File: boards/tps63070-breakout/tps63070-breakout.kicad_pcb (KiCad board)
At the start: 2 copper layers, 24.7 x 22.9 mm, 15 parts, among them J1 MODULE PINS, U1 TPS63070

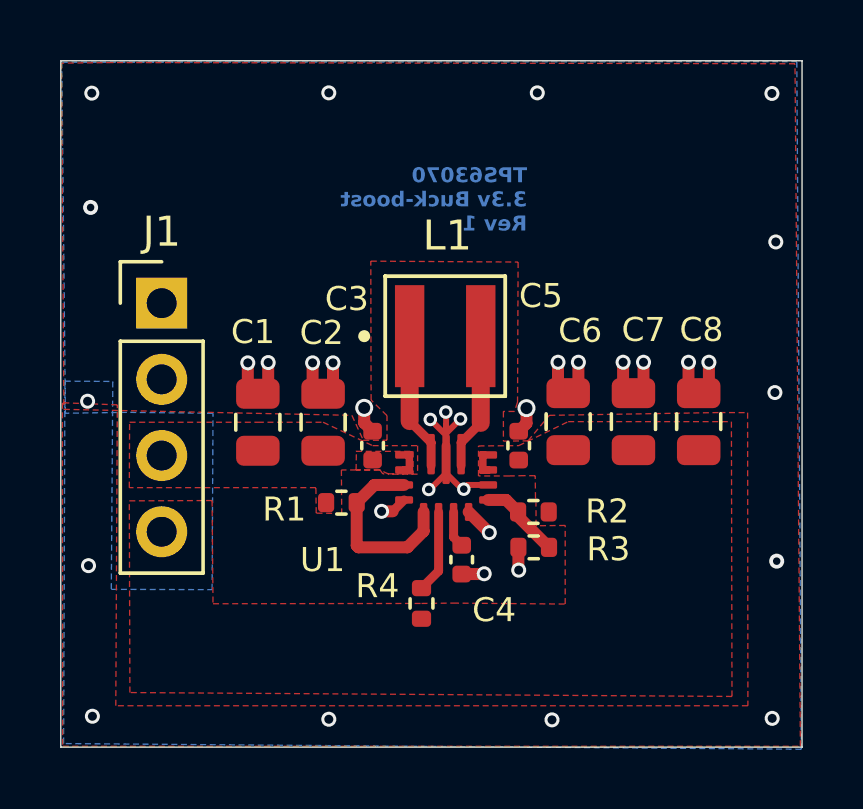
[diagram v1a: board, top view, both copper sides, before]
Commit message: fix: correct TPS63070 symbol pin types and update board docs (#24)
* fix: correct TPS63070 symbol pin types, update board README

Symbol library changes:
- VOUT pins 7/8: power_in → power_out/passive (it outputs power)
- L1/L2 pins 11/9: unspecified → passive (inductor connections)
- VAUX pin 3: unspecified → power_out (auxiliary supply)
- PGND pin 10: power_in → passive (duplicate ground pin)
- VIN pin 13: power_in → passive (duplicate input pin)

Eliminates 4 of 6 ERC violations. Remaining 2 are VIN/GND
power_pin_not_driven warnings (need PWR_FLAG in KiCad GUI).
Demoted power_pin_not_driven to warning in project file.

Board README updated with full BOM, datasheet links, resistor
divider table, and known DRC items section.

Closes #23

Made-with: Cursor

* fix: set correct footprint library reference for TPS63070 symbol

Change Footprint field from bare "RNM0015A" to "TPS63070:TPS63070"
in the library symbol, embedded schematic copy, and U1 instance.
Resolves the footprint_link_issues ERC warning — ERC now passes
with 0 violations.

Made-with: Cursor

* chore: update used_designators after adding PWR_FLAG symbols

Made-with: Cursor

* fix: remove --schematic-parity from fab DRC script

Parity is already checked by the dedicated DRC job. Running it again
during fab DRC double-counts parity issues and inflates violation
numbers in the report.

Made-with: Cursor

* chore: gitignore board-level .kicad_dru files

The fab DRC script temporarily copies rule files into board directories.
KiCad may also regenerate these on save. Ignore them to prevent
accidental commits.

Made-with: Cursor

* feat: add standard/advanced tiers for 2-layer fab rules

Rename existing 2-layer rules to *-standard and add *-advanced
variants with tighter via/drill/clearance for boards that need them.
Point tps63070-breakout at advanced targets.

Made-with: Cursor

* fix: re-suppress footprint_symbol_field_mismatch (KiCad reverted it)

KiCad resets this severity to "warning" on save. Setting back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
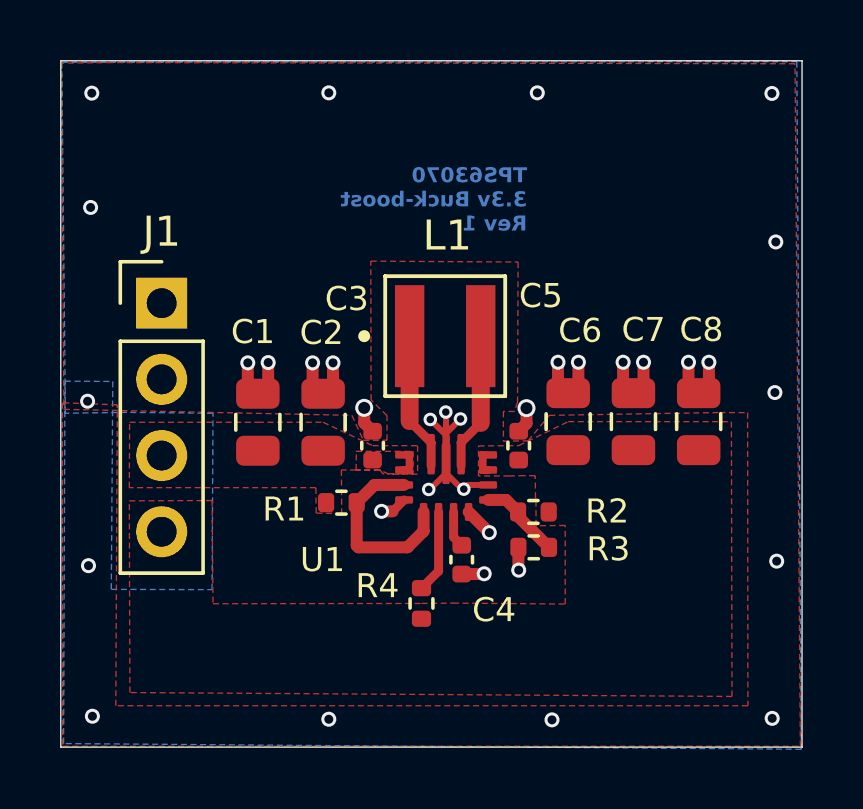
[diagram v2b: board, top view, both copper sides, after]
